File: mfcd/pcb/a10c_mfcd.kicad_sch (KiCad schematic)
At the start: 127 parts, among them J2 Conn_02x13_Odd_Even, Q1 BC817-25LT1G

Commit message: feat(mfcd): updated whole layout to use JST
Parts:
- removed J2: Conn_02x13_Odd_Even, Connector_IDC:IDC-Header_2x13_P2.54mm_Vertical_SMD, symbol Connector_Generic:Conn_02x13_Odd_Even
- added J1: Conn_LED, Connector_JST:JST_XH_B3B-XH-A_1x03_P2.50mm_Vertical, symbol Connector_Generic:Conn_01x03
- added J2: Conn_ROWS, Connector_JST:JST_XH_B10B-XH-A_1x10_P2.50mm_Vertical, symbol Connector_Generic:Conn_01x10
- added J3: Conn_COLS, Connector_JST:JST_XH_B7B-XH-A_1x07_P2.50mm_Vertical, symbol Connector_Generic:Conn_01x07
- ADJ_DWN1, ADJ_UP1, BRT_DWN1, BRT_UP1, CON_DWN1, CON_UP1, DSP_DWN1, DSP_UP1, OSB1, OSB10, OSB11, OSB12, OSB13, OSB14, OSB15, OSB16, OSB17, OSB18, OSB19, OSB2, OSB20, OSB3, OSB4, OSB5, OSB6, OSB7, OSB8, OSB9, SYM_DWN1, SYM_UP1: footprint ButtonSwitchSMDEspena:SW_SPST_TL3301_6x6mm_H4.3mm -> Mouser:18259671
- LED1, LED10, LED11, LED12, LED13, LED14, LED15, LED16, LED17, LED18, LED19, LED2, LED20, LED21, LED22, LED23, LED24, LED25, LED26, LED27, LED28, LED29, LED3, LED30, LED31, LED4, LED5, LED6, LED7, LED8, LED9: value HSMG-C150 -> 1206; symbol MOUSER:HSMG-C150 -> Device:LED
- S1: footprint SRBV131502 -> Mouser:SRBV131502
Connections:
- net 5V: now also J1.1 (Pin_1)
- net COL0: now also J3.1 (Pin_1)
- net COL1: now also J3.2 (Pin_2)
- net COL2: now also J3.3 (Pin_3)
- net COL3: now also J3.4 (Pin_4)
- net COL4: now also J3.5 (Pin_5)
- net COL5: now also J3.6 (Pin_6)
- net COL6: now also J3.7 (Pin_7)
- net GND: now also J1.3 (Pin_3)
- net LED: now also J1.2 (Pin_2)
- net ROW0: now also J2.1 (Pin_1)
- net ROW1: now also J2.2 (Pin_2)
- net ROW2: now also J2.3 (Pin_3)
- net ROW3: now also J2.4 (Pin_4)
- net ROW4: now also J2.5 (Pin_5)
- net ROW5: now also J2.6 (Pin_6)
- net ROW6: now also J2.7 (Pin_7)
- net ROW7: now also J2.8 (Pin_8)
- net ROW8: now also J2.9 (Pin_9)
- net ROW9: now also J2.10 (Pin_10)
- net at LED1.2 (A), R2.1: now also LED1.1 (K), Q1.3 (COLLECTOR)
- now unconnected: LED10.1 (K), LED11.1 (K), LED12.1 (K), LED13.1 (K), LED14.1 (K), LED15.1 (K), LED16.1 (K), LED17.1 (K), LED18.1 (K), LED19.1 (K), LED2.1 (K), LED20.1 (K), LED21.1 (K), LED22.1 (K), LED23.1 (K), LED24.1 (K), LED25.1 (K), LED26.1 (K), LED27.1 (K), LED28.1 (K), LED29.1 (K), LED3.1 (K), LED30.1 (K), LED31.1 (K), LED4.1 (K), LED5.1 (K), LED6.1 (K), LED7.1 (K), LED8.1 (K), LED9.1 (K)

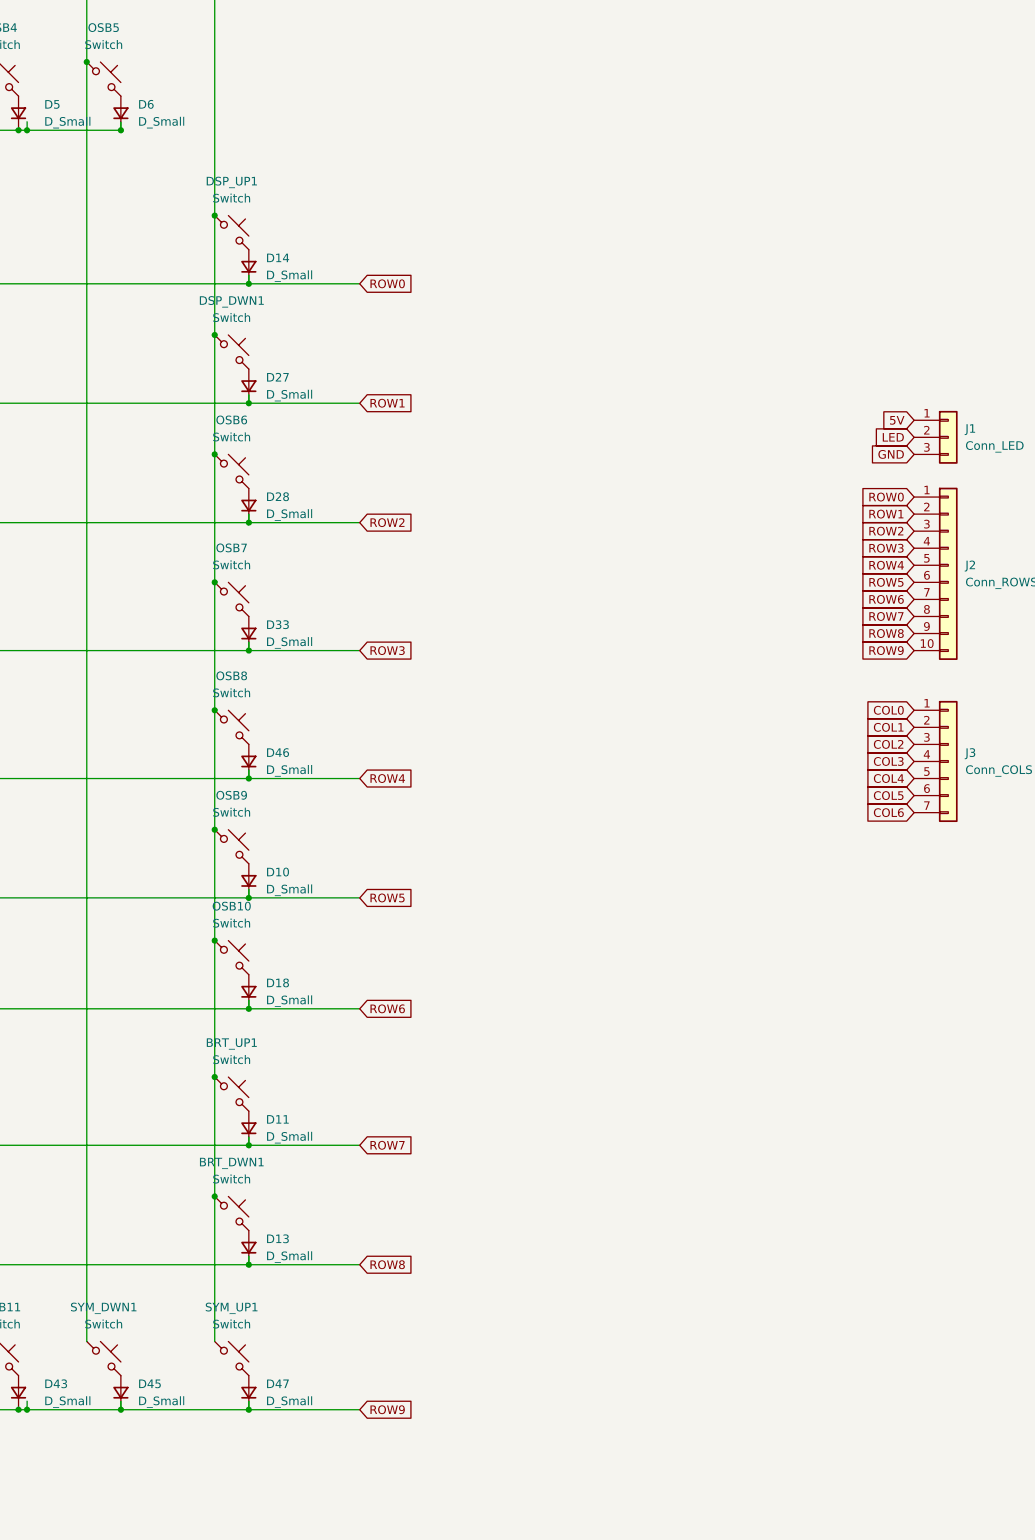
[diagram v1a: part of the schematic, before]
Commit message: feat(mfcd): added initial arduino code
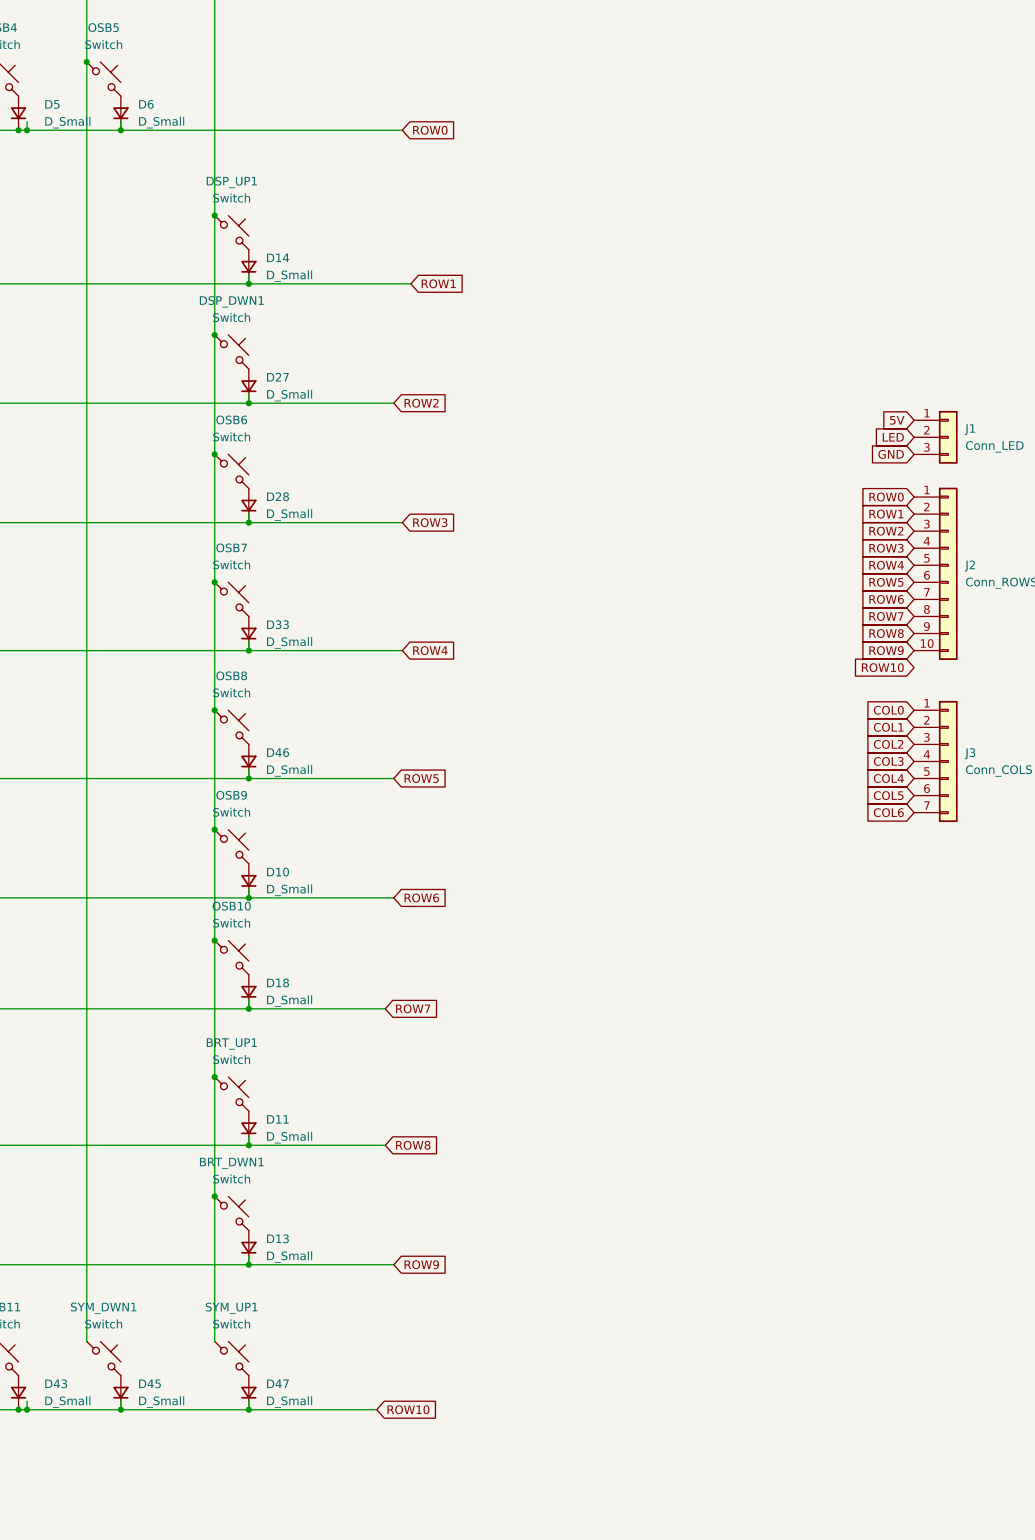
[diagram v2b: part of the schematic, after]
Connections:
- net ROW0: now also D2.1 (K), D3.1 (K), D4.1 (K), D5.1 (K), D6.1 (K); no longer D14.1 (K), D8.1 (K)
- net ROW1: now also D14.1 (K), D8.1 (K); no longer D15.1 (K), D27.1 (K)
- net ROW2: now also D15.1 (K), D27.1 (K); no longer D16.1 (K), D28.1 (K)
- net ROW3: now also D16.1 (K), D28.1 (K); no longer D1.1 (K), D33.1 (K)
- net ROW4: now also D1.1 (K), D33.1 (K); no longer D34.1 (K), D46.1 (K)
- net ROW5: now also D34.1 (K), D46.1 (K); no longer D10.1 (K), D7.1 (K)
- net ROW6: now also D10.1 (K), D7.1 (K); no longer D17.1 (K), D18.1 (K)
- net ROW7: now also D17.1 (K), D18.1 (K); no longer D11.1 (K), D9.1 (K)
- net ROW8: now also D11.1 (K), D9.1 (K); no longer D12.1 (K), D13.1 (K)
- net ROW9: now also D12.1 (K), D13.1 (K); no longer D35.1 (K), D37.1 (K), D39.1 (K), D41.1 (K), D43.1 (K), D45.1 (K), D47.1 (K)
- new net ROW10: D35.1 (K), D37.1 (K), D39.1 (K), D41.1 (K), D43.1 (K), D45.1 (K), D47.1 (K)
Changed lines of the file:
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@@
-	(wire
-		(pts
-			(xy 171.45 162.56) (xy 154.94 162.56)
-		)
-		(stroke
-			(width 0)
-			(type default)
-		)
-	)
 	(wire
 		(pts
@@
 	(wire
 		(pts
-			(xy 171.45 238.76) (xy 154.94 238.76)
-		)
-		(stroke
-			(width 0)
-			(type default)
-		)
-	)
-	(wire
-		(pts
-			(xy 171.45 217.17) (xy 154.94 217.17)
-		)
-		(stroke
-			(width 0)
-			(type default)
-		)
-	)
-	(wire
-		(pts
 			(xy 405.13 457.2) (xy 417.83 457.2)
 		)
@@
 	(wire
 		(pts
-			(xy 171.45 125.73) (xy 154.94 125.73)
-		)
-		(stroke
-			(width 0)
-			(type default)
-		)
-	)
-	(wire
-		(pts
 			(xy 69.85 237.49) (xy 69.85 238.76)
 		)
@@
 	(wire
 		(pts
+			(xy 177.8 48.26) (xy 135.89 48.26)
+		)
+		(stroke
+			(width 0)
+			(type default)
+		)
+	)
+	(wire
+		(pts
 			(xy 115.57 26.67) (xy 115.57 38.1)
 		)
@@
 	(wire
 		(pts
-			(xy 171.45 71.12) (xy 154.94 71.12)
-		)
-		(stroke
-			(width 0)
-			(type default)
-		)
-	)
-	(wire
-		(pts
 			(xy 425.45 165.1) (xy 425.45 180.34)
 		)
@@
 	(wire
 		(pts
-			(xy 171.45 179.07) (xy 154.94 179.07)
-		)
-		(stroke
-			(width 0)
-			(type default)
-		)
-	)
-	(wire
-		(pts
 			(xy 405.13 240.03) (xy 417.83 240.03)
 		)
@@
 	(wire
 		(pts
-			(xy 171.45 106.68) (xy 154.94 106.68)
-		)
-		(stroke
-			(width 0)
-			(type default)
-		)
-	)
-	(wire
-		(pts
 			(xy 49.53 162.56) (xy 154.94 162.56)
 		)
@@
 	(wire
 		(pts
+			(xy 175.26 199.39) (xy 154.94 199.39)
+		)
+		(stroke
+			(width 0)
+			(type default)
+		)
+	)
+	(wire
+		(pts
 			(xy 154.94 237.49) (xy 154.94 238.76)
 		)
@@
 	(wire
 		(pts
+			(xy 176.53 144.78) (xy 154.94 144.78)
+		)
+		(stroke
+			(width 0)
+			(type default)
+		)
+	)
+	(wire
+		(pts
 			(xy 87.63 48.26) (xy 105.41 48.26)
 		)
@@
 	(wire
 		(pts
+			(xy 176.53 88.9) (xy 154.94 88.9)
+		)
+		(stroke
+			(width 0)
+			(type default)
+		)
+	)
+	(wire
+		(pts
 			(xy 44.45 25.4) (xy 44.45 60.96)
 		)
@@
 	(wire
 		(pts
-			(xy 171.45 144.78) (xy 154.94 144.78)
-		)
-		(stroke
-			(width 0)
-			(type default)
-		)
-	)
-	(wire
-		(pts
 			(xy 405.13 518.16) (xy 417.83 518.16)
 		)
@@
 	(wire
 		(pts
-			(xy 171.45 199.39) (xy 154.94 199.39)
-		)
-		(stroke
-			(width 0)
-			(type default)
-		)
-	)
-	(wire
-		(pts
 			(xy 49.53 237.49) (xy 49.53 238.76)
 		)
@@
 	(wire
 		(pts
+			(xy 175.26 179.07) (xy 154.94 179.07)
+		)
+		(stroke
+			(width 0)
+			(type default)
+		)
+	)
+	(wire
+		(pts
 			(xy 121.92 48.26) (xy 135.89 48.26)
 		)
@@
 	(wire
 		(pts
+			(xy 173.99 238.76) (xy 154.94 238.76)
+		)
+		(stroke
+			(width 0)
+			(type default)
+		)
+	)
+	(wire
+		(pts
 			(xy 44.45 189.23) (xy 44.45 207.01)
 		)
@@
 	(wire
 		(pts
+			(xy 177.8 106.68) (xy 154.94 106.68)
+		)
+		(stroke
+			(width 0)
+			(type default)
+		)
+	)
+	(wire
+		(pts
 			(xy 44.45 96.52) (xy 44.45 115.57)
 		)
@@
 	(wire
 		(pts
+			(xy 176.53 162.56) (xy 154.94 162.56)
+		)
+		(stroke
+			(width 0)
+			(type default)
+		)
+	)
+	(wire
+		(pts
 			(xy 425.45 518.16) (xy 425.45 532.13)
 		)
@@
 	(wire
 		(pts
-			(xy 171.45 88.9) (xy 154.94 88.9)
+			(xy 176.53 217.17) (xy 154.94 217.17)
 		)
 		(stroke
@@
 	(wire
 		(pts
+			(xy 177.8 125.73) (xy 154.94 125.73)
+		)
+		(stroke
+			(width 0)
+			(type default)
+		)
+	)
+	(wire
+		(pts
 			(xy 44.45 60.96) (xy 44.45 78.74)
 		)
@@
 		(pts
 			(xy 425.45 532.13) (xy 425.45 547.37)
+		)
+		(stroke
+			(width 0)
+			(type default)
+		)
+	)
+	(wire
+		(pts
+			(xy 179.07 71.12) (xy 154.94 71.12)
 		)
 		(stroke
@@
 	(global_label "ROW9"
 		(shape input)
-		(at 171.45 238.76 0)
+		(at 176.53 217.17 0)
 		(fields_autoplaced yes)
 		(effects
@@
 		)
 		(property "Intersheetrefs" "${INTERSHEET_REFS}"
-			(at 179.6966 238.76 0)
+			(at 184.7766 217.17 0)
 			(effects
 				(font
@@
 	(global_label "ROW8"
 		(shape input)
-		(at 171.45 217.17 0)
+		(at 175.26 199.39 0)
 		(fields_autoplaced yes)
 		(effects
@@
 		)
 		(property "Intersheetrefs" "${INTERSHEET_REFS}"
-			(at 179.6966 217.17 0)
+			(at 183.5066 199.39 0)
 			(effects
 				(font
@@
 	(global_label "ROW1"
 		(shape input)
-		(at 171.45 88.9 0)
+		(at 179.07 71.12 0)
 		(fields_autoplaced yes)
 		(effects
@@
 		)
 		(property "Intersheetrefs" "${INTERSHEET_REFS}"
-			(at 179.6966 88.9 0)
+			(at 187.3166 71.12 0)
 			(effects
 				(font
@@
 	(global_label "ROW2"
 		(shape input)
-		(at 171.45 106.68 0)
+		(at 176.53 88.9 0)
 		(fields_autoplaced yes)
 		(effects
@@
 		)
 		(property "Intersheetrefs" "${INTERSHEET_REFS}"
-			(at 179.6966 106.68 0)
+			(at 184.7766 88.9 0)
 			(effects
 				(font
@@
 	(global_label "ROW6"
 		(shape input)
-		(at 171.45 179.07 0)
+		(at 176.53 162.56 0)
 		(fields_autoplaced yes)
 		(effects
@@
 		)
 		(property "Intersheetrefs" "${INTERSHEET_REFS}"
-			(at 179.6966 179.07 0)
+			(at 184.7766 162.56 0)
 			(effects
 				(font
@@
 		)
 	)
+	(global_label "ROW10"
+		(shape input)
+		(at 173.99 238.76 0)
+		(fields_autoplaced yes)
+		(effects
+			(font
+				(size 1.27 1.27)
+			)
+			(justify left)
+		)
+		(property "Intersheetrefs" "${INTERSHEET_REFS}"
+			(at 183.4461 238.76 0)
+			(effects
+				(font
+					(size 1.27 1.27)
+				)
+				(justify left)
+				(hide yes)
+			)
+		)
+	)
 	(global_label "ROW4"
 		(shape input)
-		(at 171.45 144.78 0)
+		(at 177.8 125.73 0)
 		(fields_autoplaced yes)
 		(effects
@@
 		)
 		(property "Intersheetrefs" "${INTERSHEET_REFS}"
-			(at 179.6966 144.78 0)
+			(at 186.0466 125.73 0)
 			(effects
 				(font
@@
 		)
 	)
+	(global_label "ROW10"
+		(shape input)
+		(at 254 128.27 180)
+		(fields_autoplaced yes)
+		(effects
+			(font
+				(size 1.27 1.27)
+			)
+			(justify right)
+		)
+		(property "Intersheetrefs" "${INTERSHEET_REFS}"
+			(at 244.5439 128.27 0)
+			(effects
+				(font
+					(size 1.27 1.27)
+				)
+				(justify right)
+				(hide yes)
+			)
+		)
+	)
 	(global_label "ROW0"
 		(shape input)
-		(at 171.45 71.12 0)
+		(at 177.8 48.26 0)
 		(fields_autoplaced yes)
 		(effects
@@
 		)
 		(property "Intersheetrefs" "${INTERSHEET_REFS}"
-			(at 179.6966 71.12 0)
+			(at 186.0466 48.26 0)
 			(effects
 				(font
@@
 	(global_label "ROW3"
 		(shape input)
-		(at 171.45 125.73 0)
+		(at 177.8 106.68 0)
 		(fields_autoplaced yes)
 		(effects
@@
 		)
 		(property "Intersheetrefs" "${INTERSHEET_REFS}"
-			(at 179.6966 125.73 0)
+			(at 186.0466 106.68 0)
 			(effects
 				(font
@@
 	(global_label "ROW7"
 		(shape input)
-		(at 171.45 199.39 0)
+		(at 175.26 179.07 0)
 		(fields_autoplaced yes)
 		(effects
@@
 		)
 		(property "Intersheetrefs" "${INTERSHEET_REFS}"
-			(at 179.6966 199.39 0)
+			(at 183.5066 179.07 0)
 			(effects
 				(font
@@
 	(global_label "ROW5"
 		(shape input)
-		(at 171.45 162.56 0)
+		(at 176.53 144.78 0)
 		(fields_autoplaced yes)
 		(effects
@@
 		)
 		(property "Intersheetrefs" "${INTERSHEET_REFS}"
-			(at 179.6966 162.56 0)
-			(effects
-				(font
+			(at 184.7766 144.78 0)
+			(effects
+				(font
